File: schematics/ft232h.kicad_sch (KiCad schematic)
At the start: 4 parts, among them Q2 2N7000, U38 ATF22V10C-7

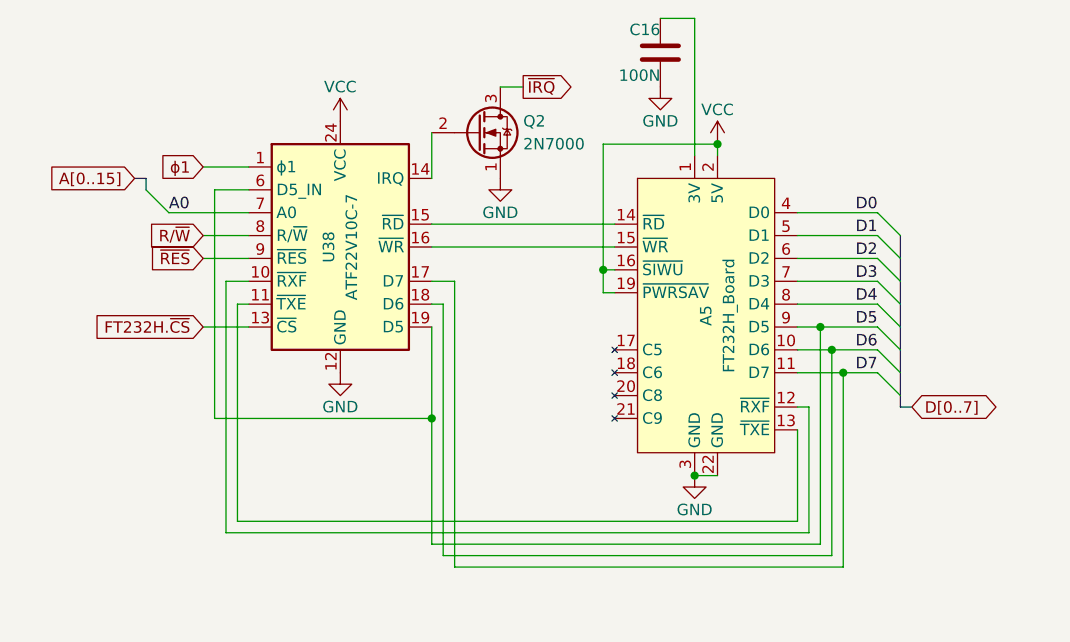
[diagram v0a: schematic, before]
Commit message: new ft245 support
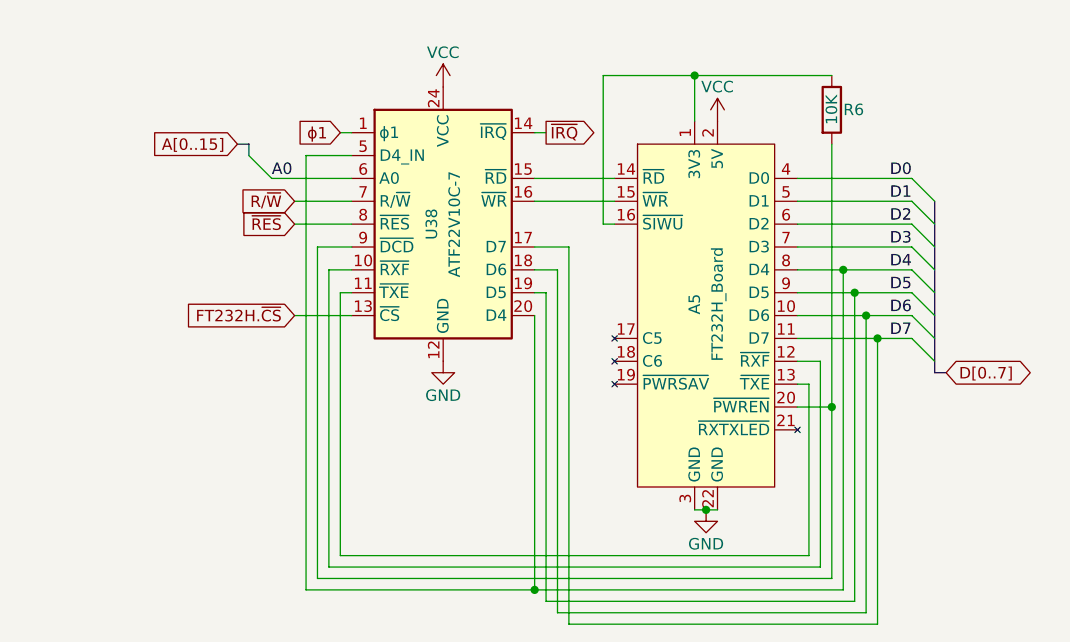
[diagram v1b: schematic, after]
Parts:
- removed C16: 100N, symbol Device:C
- removed Q2: 2N7000, Package_TO_SOT_THT:TO-92_Inline, symbol Transistor_FET:2N7000
- added R6: 10K, symbol Device:R
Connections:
- net A0: now also U38.6 (A0); no longer U38.7 (A0)
- net D4: now also U38.20 (D4), U38.5 (D4_IN)
- net D5: no longer U38.6 (D5_IN)
- net R/~{W}: now also U38.7 (R/~{W}); no longer U38.8 (R/~{W})
- net VCC: no longer A5.16 (~{SIWU}), A5.19 (~{PWRSAV})
- net ~{IRQ}: now also U38.14 (~{IRQ})
- net ~{RES}: now also U38.8 (~{RES}); no longer U38.9 (~{RES})
- net at A5.1 (3V3): now also A5.16 (~{SIWU}), R6.1
- net at A5.20 (~{PWREN}): now also U38.9 (~{DCD}), R6.2
